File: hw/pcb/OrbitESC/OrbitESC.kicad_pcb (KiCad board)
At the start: 4 copper layers, 75 x 30 mm, 225 parts, among them J1 USB_C_Receptacle_USB2.0, J11 VDC, J12 GND, J2 Micro_SD_Card_Det, J3 TermA, J4 TermB, J5 TermC, J6 CAN1, J7 Serial1, J8 Serial2, J9 CAN2, Q1 MCAC80N10Y, Q2 MCAC80N10Y, Q3 MCAC80N10Y, Q4 MCAC80N10Y, Q5 MCAC80N10Y, Q6 MCAC80N10Y, Q7 2N7002, SW1 Reset, SW2 User, SW3 Boot, SW4 Break, U1 TLE9250X, U10 TLE9250X, U2 AT25SF081-SSHD-X, U3 24LC128, U4 STM32F446ZCHx, U5 DRV8300DRGER, U6 TSV994, U7 AP62200Z6-7, U8 AP2171W, U9 AP2120, X1 ECS-2520MV-240-BN

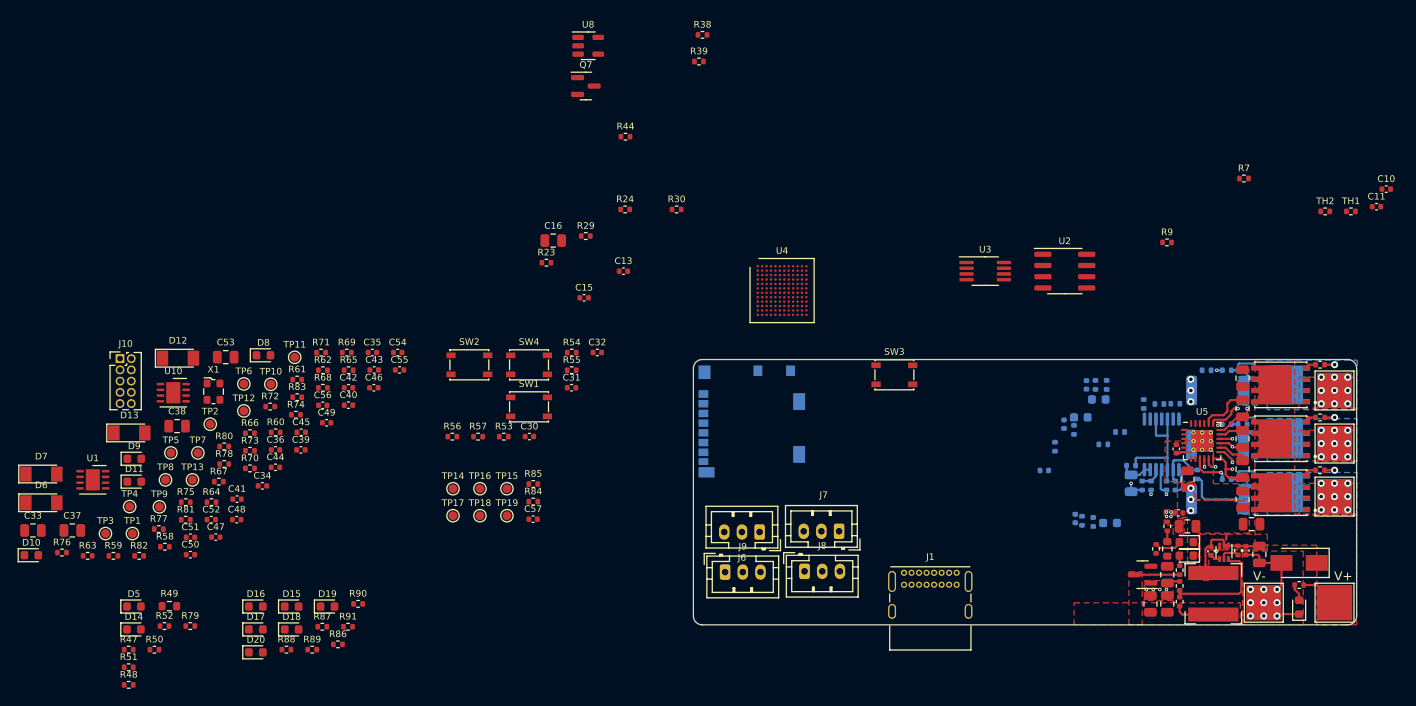
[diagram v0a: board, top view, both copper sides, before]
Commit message: Route analogs and power stage sections
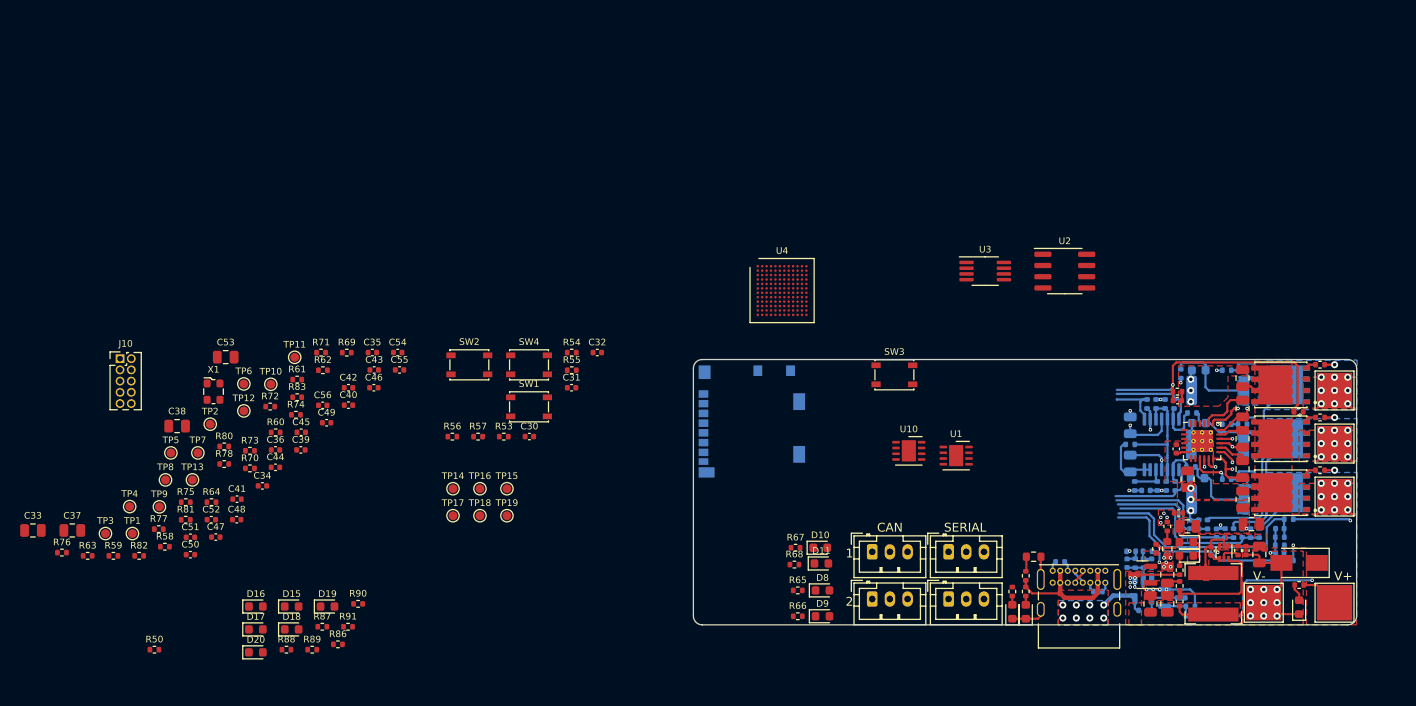
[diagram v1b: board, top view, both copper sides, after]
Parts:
- removed D12, D13, D6, D7: 3.3V, Diode_SMD:D_MiniMELF
- C10, C13, C15, C16, C57, Q7, R23, R24, R29, R30, R38, R39, R44, R51, R52, R7, R84, R85, TH1, U8: moved to B.Cu
- moved R51 106.0 mm to (144.5, 106.9), turned to 180 degrees
- moved R52 105.6 mm to (148.7, 110.2)
- moved R48 102.2 mm to (140.6, 108.5), turned to 90 degrees
- moved R47 101.7 mm to (140.6, 110.2), turned to -90 degrees
- moved D5 100.9 mm to (140.6, 112.5), turned to 90 degrees
- moved D14 99.4 mm to (139.1, 112.5), turned to 90 degrees
- moved R49 97.9 mm to (141.5, 106.3)
- moved U1 97.7 mm to (132.7, 94.9)
- moved R79 93.0 mm to (139.1, 110.2), turned to -90 degrees
- moved R23 90.5 mm to (170.3, 106.7)
- moved D10 89.2 mm to (117.3, 105.3)
- moved Q7 88.1 mm to (157.2, 110.9)
- moved U8 87.8 mm to (153.9, 109.9), turned to -90 degrees
- moved R38 85.0 mm to (159.2, 111.9), turned to 180 degrees
- moved R39 83.8 mm to (159.2, 113.0), turned to 180 degrees
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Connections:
- TH1 pad 1: +3.3V -> +3.3VADC
- TH2 pad 1: +3.3V -> +3.3VADC
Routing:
- net GND: track 23.0 -> 58.9 mm, vias 22 -> 27
- net /MCU/TEMP_VB: track 0.00 -> 30.5 mm, vias 0 -> 1
- net /MCU/TEMP_VA: track 0.00 -> 25.9 mm
- net /MCU/INPUT_VOLTAGE: track 0.00 -> 23.6 mm
- net /Outputs and Shunts/SH_A: track 13.3 -> 35.6 mm
- net VBUS: track 0.00 -> 20.4 mm, vias 0 -> 8
- net VDC: track 7.86 -> 27.9 mm, vias 0 -> 2
- net /MCU/MOTOR_VC: track 0.00 -> 19.5 mm
- net /MCU/MOTOR_VB: track 0.00 -> 16.3 mm
- net /Outputs and Shunts/SH_B: track 13.0 -> 27.3 mm
- net +3.3VADC: track 0.49 -> 14.5 mm, vias 5 -> 8
- net /MCU/MOTOR_VA: track 0.00 -> 13.1 mm
- net Net-(R34-Pad2): track 0.00 -> 11.5 mm, vias 0 -> 2
- net /Outputs and Shunts/A_ISENSE_P: track 1.62 -> 12.2 mm
- net /MCU/MOTOR_IB: track 0.00 -> 9.88 mm
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- added copper zone on F.Cu, net +3.3V
- added copper zone on In2.Cu, net +3.3V
- added copper zone on In2.Cu, net +5V
- added copper zone on B.Cu, net VBUS
- added copper zone on F.Cu, net VBUS
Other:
- board text added: "1"
- board text added: "2"
- board text added: "CAN"
- board text added: "SERIAL"

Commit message: Tentative component placement for remainder pieces
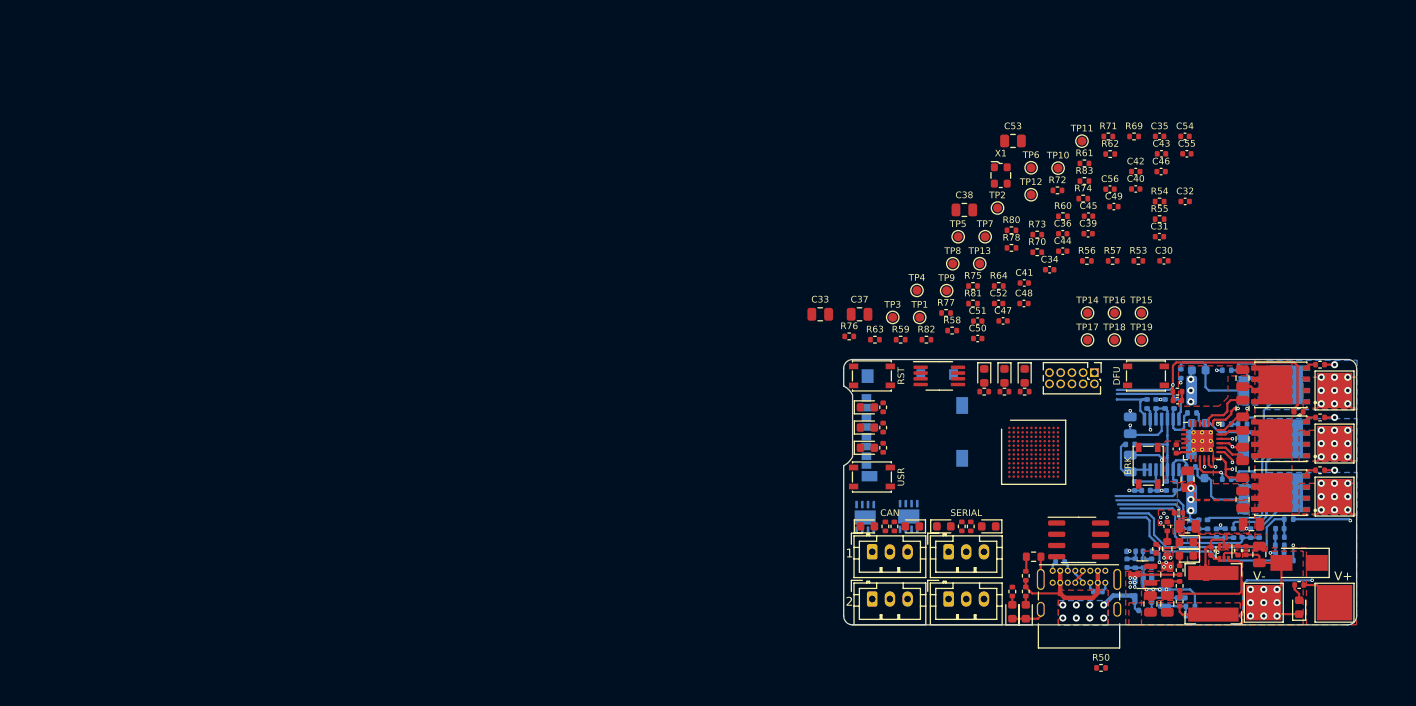
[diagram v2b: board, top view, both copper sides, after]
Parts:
- U1, U10: moved to B.Cu
- moved J10 110.2 mm to (148.3, 85.5), turned to -90 degrees
- moved R50 107.1 mm to (149.1, 118.9)
- moved C35 92.3 mm to (155.7, 58.8)
- moved C48 92.3 mm to (140.4, 77.7)
- moved C54 92.3 mm to (158.6, 58.8)
- moved R61 92.3 mm to (147.2, 61.8)
- moved R62 92.3 mm to (150.1, 60.8)
- moved R64 92.3 mm to (137.5, 75.7)
- moved R70 92.3 mm to (141.9, 71.9)
- moved R73 92.3 mm to (141.9, 69.9)
- moved R75 92.3 mm to (134.6, 75.7)
- moved R78 92.3 mm to (139.0, 71.4)
- moved R80 92.3 mm to (139.0, 69.4)
- moved R81 92.3 mm to (134.6, 77.7)
- moved R83 92.3 mm to (147.2, 63.8)
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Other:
- board size 75 x 30 mm -> 58 x 30 mm
- board text added: "BRK"
- board text added: "DFU"
- board text added: "RST"
- board text added: "USR"

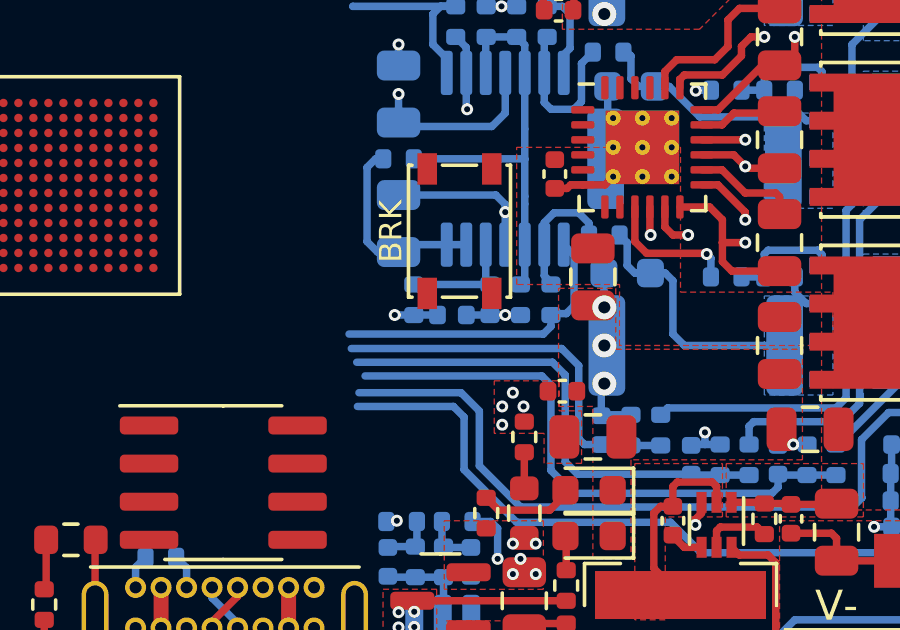
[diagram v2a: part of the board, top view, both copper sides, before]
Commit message: Start rework of processor selection after realizing I can't afford manufacturing...
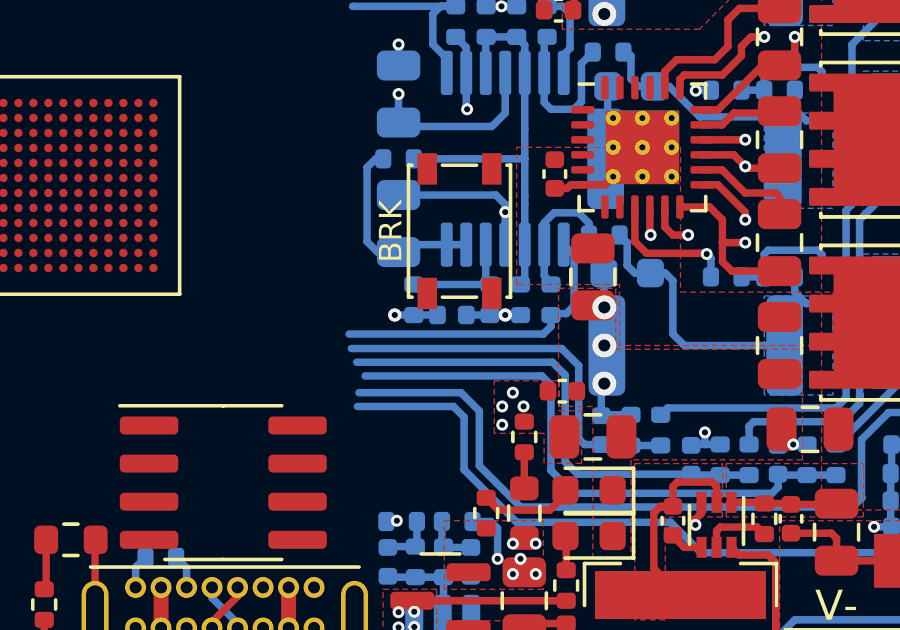
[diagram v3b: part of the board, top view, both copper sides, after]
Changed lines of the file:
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@@
   (via (at 169 110) (size 0.8) (drill 0.4) (layers "F.Cu" "B.Cu") (net 158))
   (via (at 166 111.5) (size 0.8) (drill 0.4) (layers "F.Cu" "B.Cu") (net 158))
-  (via (at 155.956 98.806) (size 0.4) (drill 0.2) (layers "F.Cu" "B.Cu") (net 158))
+  (via (at 155.956 98.806) (size 0.45) (drill 0.2) (layers "F.Cu" "B.Cu") (net 158))
   (via (at 155 110) (size 0.4) (drill 0.2) (layers "F.Cu" "B.Cu") (free) (net 158))
   (via (at 166 110) (size 0.8) (drill 0.4) (layers "F.Cu" "B.Cu") (net 158))
@@
   (segment (start 171.958 89.916) (end 171.577 90.297) (width 0.25) (layer "F.Cu") (net 183))
   (segment (start 171.96 89.916) (end 171.958 89.916) (width 0.25) (layer "F.Cu") (net 183))
-  (via (at 152.273 98.806) (size 0.4) (drill 0.2) (layers "F.Cu" "B.Cu") (net 183))
+  (via (at 152.273 98.806) (size 0.45) (drill 0.2) (layers "F.Cu" "B.Cu") (net 183))
   (via (at 177.292 102.2096) (size 0.4) (drill 0.2) (layers "F.Cu" "B.Cu") (net 183))
   (via (at 152.4 91.44) (size 0.4) (drill 0.2) (layers "F.Cu" "B.Cu") (net 183))

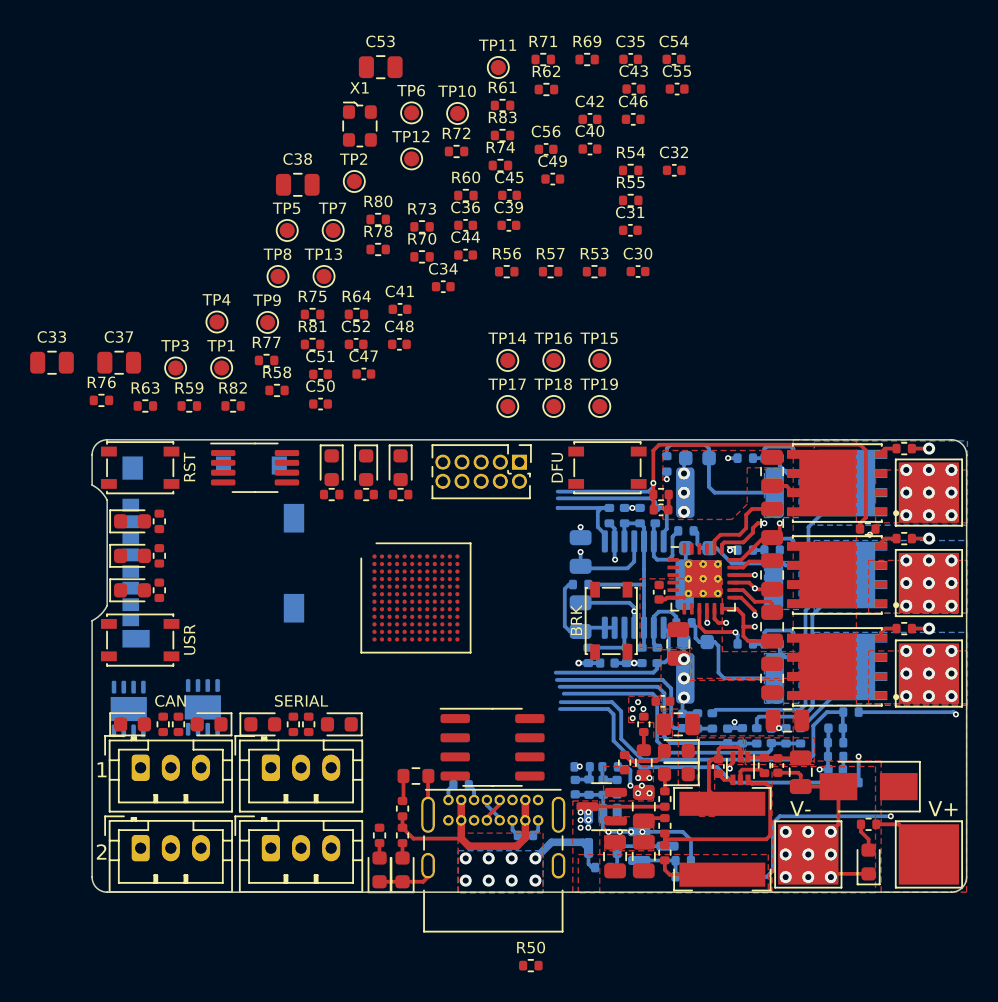
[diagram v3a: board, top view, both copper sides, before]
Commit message: Rework new processor
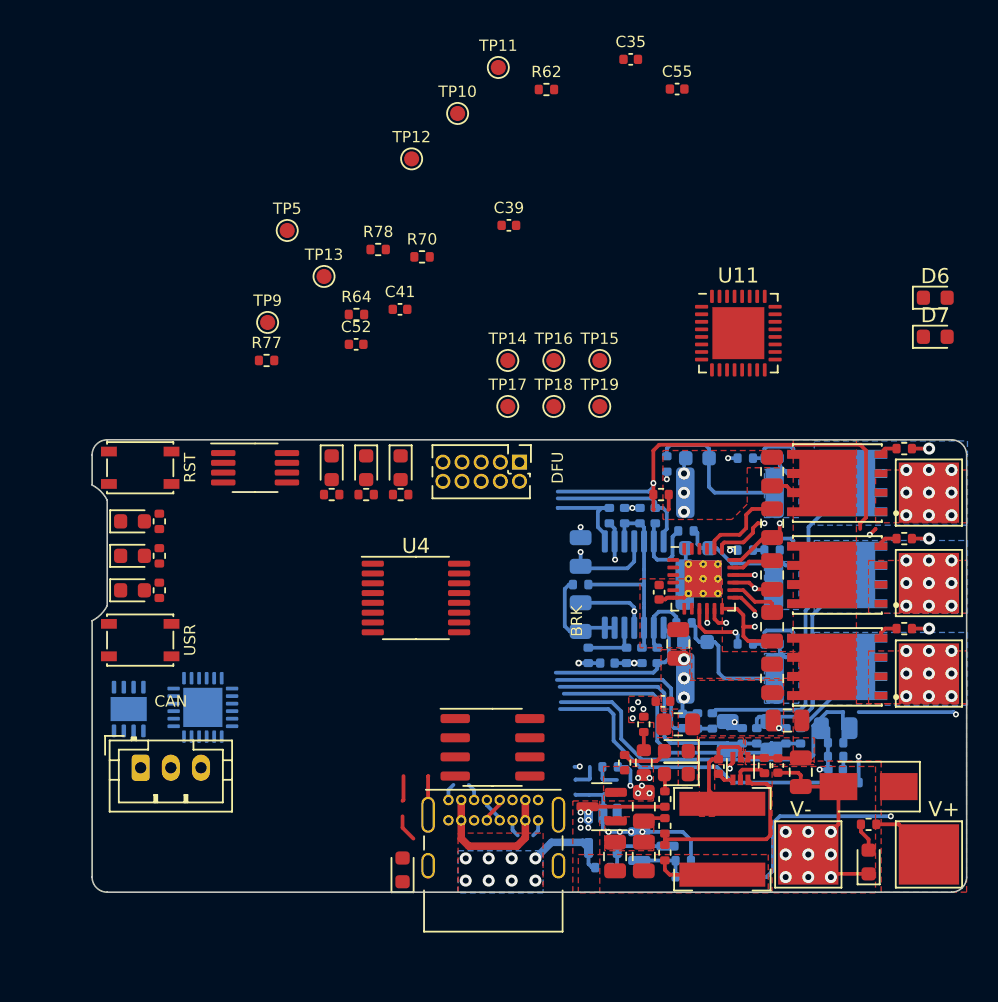
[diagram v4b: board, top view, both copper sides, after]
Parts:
- removed C11: 1uF, Capacitor_SMD:C_0402_1005Metric
- removed C15, C30, C31, C32, C34, C36, C40, C42, C43, C44, C45, C46, C47, C48, C49, C50, C51, C54, C56, C57: 100nF, Capacitor_SMD:C_0402_1005Metric
- removed C33, C37, C38, C53: 2.2uF, Capacitor_SMD:C_0805_2012Metric
- removed D10, D11, D14, D8, D9: Yellow LED, Diode_SMD:D_0603_1608Metric
- removed J2: Micro_SD_Card_Det, Connector_Card:microSD_HC_Molex_104031-0811
- removed J7: Serial1, Connector_JST:JST_PH_B3B-PH-K_1x03_P2.00mm_Vertical
- removed J8: Serial2, Connector_JST:JST_PH_B3B-PH-K_1x03_P2.00mm_Vertical
- removed J9: CAN2, Connector_JST:JST_PH_B3B-PH-K_1x03_P2.00mm_Vertical
- removed R30, R53, R54, R55, R56, R57, R69, R71, R84, R85: 10k, Resistor_SMD:R_0402_1005Metric
- removed R47: 200, Resistor_SMD:R_0402_1005Metric
- removed R48: 33k, Resistor_SMD:R_0402_1005Metric
- removed R49: 82k, Resistor_SMD:R_0603_1608Metric
- removed R50, R58, R59, R60, R61, R65, R66, R67, R68, R79: 1.5k, Resistor_SMD:R_0402_1005Metric
- removed R51, R52: 5.1k, Resistor_SMD:R_0402_1005Metric
- removed R63: 120, Resistor_SMD:R_0402_1005Metric
- removed R72, R73, R74, R75, R76: 39k, Resistor_SMD:R_0402_1005Metric
- removed R80, R81, R82, R83: 100k, Resistor_SMD:R_0402_1005Metric
- removed SW3: Boot, Button_Switch_SMD:SW_SPST_PTS810
- removed SW4: Break, Button_Switch_SMD:SW_SPST_PTS810
- removed TH1, TH2: 10k NTC, Resistor_SMD:R_0402_1005Metric
- removed TP1: SDIO_CMD, TestPoint:TestPoint_Pad_D1.0mm
- removed TP2: SDIO_DATA_2, TestPoint:TestPoint_Pad_D1.0mm
- removed TP3: SDIO_DATA_0, TestPoint:TestPoint_Pad_D1.0mm
- removed TP4: SDIO_CARD_DETECT, TestPoint:TestPoint_Pad_D1.0mm
- removed TP6: SDIO_DATA_3, TestPoint:TestPoint_Pad_D1.0mm
- removed TP7: SDIO_CLK, TestPoint:TestPoint_Pad_D1.0mm
- removed TP8: SDIO_DATA_1, TestPoint:TestPoint_Pad_D1.0mm
- removed X1: ECS-2520MV-240-BN, Oscillator:Oscillator_SMD_ECS_2520MV-xxx-xx-4Pin_2.5x2.0mm
- added D6: Yellow LED, Diode_SMD:D_0603_1608Metric, F.Cu at (175.9, 74.6)
- added D7: Yellow LED, Diode_SMD:D_0603_1608Metric, F.Cu at (175.9, 77.2)
- added U11: STM32L432KBUx, Package_DFN_QFN:QFN-32-1EP_5x5mm_P0.5mm_EP3.45x3.45mm, F.Cu at (162.9, 76.9)
- C10: value 1uF -> 2.2uF; footprint Capacitor_SMD:C_0402_1005Metric -> Capacitor_SMD:C_0805_2012Metric
- C4, C7: value 100nF -> 2.2uF; footprint Capacitor_SMD:C_0402_1005Metric -> Capacitor_SMD:C_0805_2012Metric
- D5: value Blue LED -> Yellow LED
- R1: value 1k -> 10k
- R13: value 1k -> 5.1k
- R19: value 1k -> 1.5k
- R20, R7: value 10k -> 1.5k
- R9: value 10k -> 5.1k
- SW2: value User -> Boot
- U10: value TLE9250X -> CP2104; footprint Package_SON:HVSON-8-1EP_3x3mm_P0.65mm_EP1.6x2.4mm -> Package_DFN_QFN:QFN-24-1EP_4x4mm_P0.5mm_EP2.6x2.6mm
- U4: value STM32F446ZCHx -> 74HC596; footprint Package_BGA:UFBGA-144_7x7mm_Layout12x12_P0.5mm -> Package_SO:TSSOP-16_4.4x5mm_P0.65mm
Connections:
- C1 pad 1: /MCU/MOTOR_VA -> GND
- C1 pad 2: GND -> nRESET
- C10 pad 1: /MCU/TEMP_VA -> GND
- C10 pad 2: GND -> Net-(C10-Pad2)
- C4 pad 1: /MCU/MOTOR_VB -> GND
- C4 pad 2: GND -> VBUS
- C7 pad 1: /MCU/MOTOR_VC -> GND
- C7 pad 2: GND -> Net-(C10-Pad2)
- J10 pad 2: JTAG_TMS -> SWDIO
- J10 pad 4: JTAG_TCLK -> SWCLK
- J10 pad 6: JTAG_TDO -> unconnected-(J10-Pad6)
- J10 pad 8: JTAG_TDI -> unconnected-(J10-Pad8)
- R1 pad 1: GND -> nRESET
- R1 pad 2: /MCU/MOTOR_VA -> +3.3V
- R13 pad 1: GND -> Net-(J1-PadB5)
- R13 pad 2: /MCU/MOTOR_VB -> GND
- R15 pad 1: /MCU/MOTOR_VB -> SERIAL1_RST
- R15 pad 2: /Outputs and Shunts/SH_B -> +3.3V
- R19 pad 1: GND -> +3.3V
- R19 pad 2: /MCU/MOTOR_VC -> Net-(D6-Pad2)
- R20 pad 1: /MCU/MOTOR_VC -> +3.3V
- R20 pad 2: /Outputs and Shunts/SH_C -> Net-(D7-Pad2)
- R29 pad 1: /MCU/+3V3_VOLTAGE -> LED_nCS
- R3 pad 1: /MCU/MOTOR_VA -> GND
- R3 pad 2: /Outputs and Shunts/SH_A -> BOOT0
- R7 pad 1: /MCU/TEMP_VA -> /MCU/Status LEDs/CAN1_ACTV
- R7 pad 2: GND -> Net-(D5-Pad2)
- R86 pad 2: ARMED_LED -> /MCU/Status LEDs/HEARTBEAT
- R87 pad 1: STATUS_0_LED -> /MCU/Status LEDs/STATUS_2
- R88 pad 1: STATUS_1_LED -> /MCU/Status LEDs/STATUS_1
- R89 pad 2: HEARTBEAT_LED -> /MCU/Status LEDs/ARMED
- R9 pad 1: /MCU/TEMP_VB -> GND
- R9 pad 2: GND -> Net-(J1-PadA5)
- R90 pad 1: STATUS_2_LED -> /MCU/Status LEDs/STATUS_0
- R91 pad 1: FAULT_LED -> /MCU/Status LEDs/FAULT
- SW2 pad 1: USER_BTN -> BOOT0
- SW2 pad 2: GND -> +3.3V
- U10 pad 1: CAN2_TXD -> unconnected-(U10-Pad1)
- U10 pad 3: +5V -> USB_D+
- U10 pad 4: CAN2_RXD -> USB_D-
- U10 pad 6: Net-(J9-Pad3) -> unconnected-(U10-Pad6)
- U10 pad 7: Net-(J9-Pad1) -> VBUS
- U10 pad 8: unconnected-(U10-Pad8) -> VBUS
- U10 pad 9: GND -> SERIAL1_RST
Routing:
- net GND: track 58.9 -> 158.8 mm
- net /MCU/TEMP_VB: track 30.5 -> 0.00 mm, vias 1 -> 0
- net /MCU/TEMP_VA: track 25.9 -> 0.00 mm
- net /MCU/MOTOR_VC: track 19.5 -> 0.00 mm
- net /MCU/MOTOR_VB: track 16.3 -> 0.00 mm
- net /MCU/MOTOR_VA: track 13.1 -> 0.00 mm
- net VBUS: track 20.4 -> 17.3 mm
- net LED_nCS: track 0.00 -> 1.78 mm
- net /MCU/+3V3_VOLTAGE: track 1.78 -> 0.00 mm
- net Net-(J1-PadA5): track 1.15 -> 2.18 mm
- net Net-(D5-Pad2): track 0.99 -> 0.00 mm
- net Net-(D14-Pad2): track 0.99 -> 0.00 mm
- net /Outputs and Shunts/SH_B: track 27.3 -> 28.3 mm, vias 10 -> 11
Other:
- board text removed: "1"
- board text removed: "2"
- board text removed: "SERIAL"
